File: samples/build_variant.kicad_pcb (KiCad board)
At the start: 2 copper layers, 25 x 12 mm, 2 parts

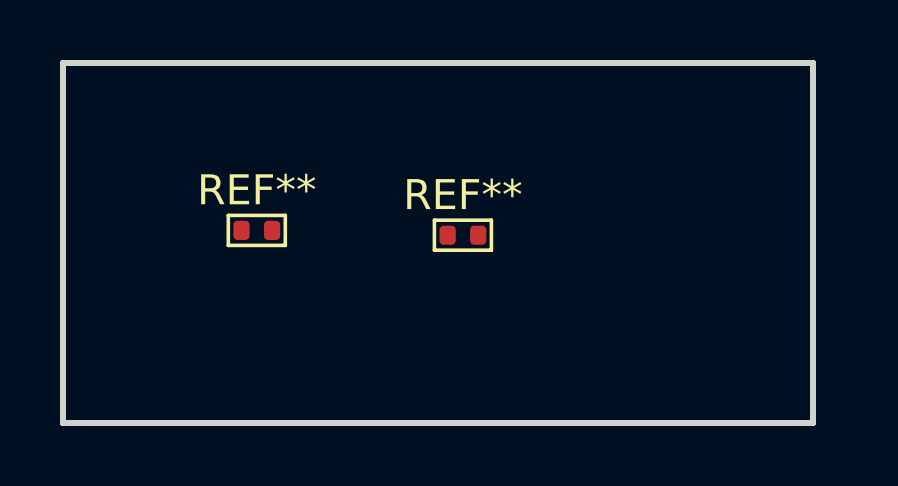
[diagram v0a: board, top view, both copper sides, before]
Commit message: Implement StringTemplate footprint & formatting
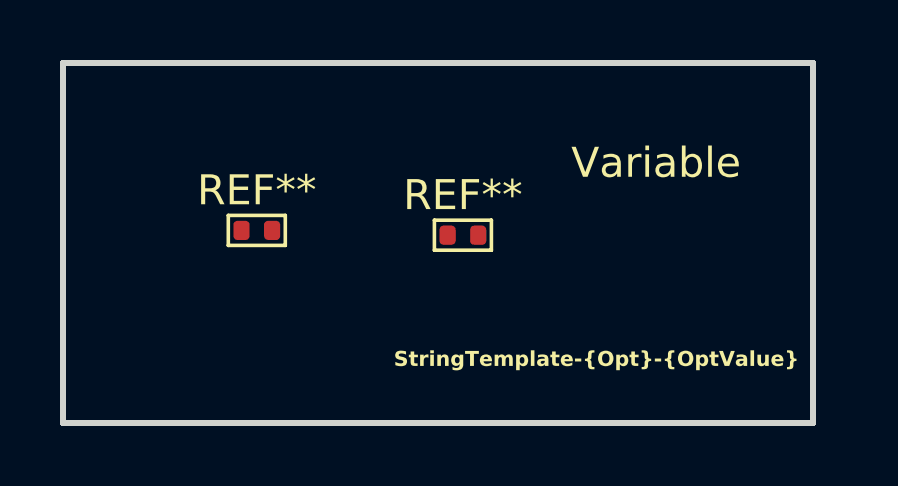
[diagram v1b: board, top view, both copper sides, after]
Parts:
- added REF**: StringTemplate-{Opt}-{OptValue}, Kikakuka:StringTemplate, F.Cu at (117.8, 109.9)
- added REF**: Variable, Kikakuka:Variable, F.Cu at (119.8, 103.3)
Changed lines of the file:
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@@
 (kicad_pcb
-	(version 20241229)
+	(version 20260206)
 	(generator "pcbnew")
-	(generator_version "9.0")
+	(generator_version "10.0")
 	(general
 		(thickness 1.6)
@@
 		(pad_to_mask_clearance 0)
 		(allow_soldermask_bridges_in_footprints no)
-		(tenting front back)
+		(tenting
+			(front yes)
+			(back yes)
+		)
+		(covering
+			(front no)
+			(back no)
+		)
+		(plugging
+			(front no)
+			(back no)
+		)
+		(capping no)
+		(filling no)
 		(pcbplotparams
 			(layerselection 0x00000000_00000000_55555555_5755f5ff)
@@
 			(usegerberadvancedattributes yes)
 			(creategerberjobfile yes)
-			(dashed_line_dash_ratio 12.000000)
-			(dashed_line_gap_ratio 3.000000)
+			(dashed_line_dash_ratio 12)
+			(dashed_line_gap_ratio 3)
 			(svgprecision 4)
 			(plotframeref no)
 			(mode 1)
 			(useauxorigin no)
-			(hpglpennumber 1)
-			(hpglpenspeed 20)
-			(hpglpendiameter 15.000000)
 			(pdf_front_fp_property_popups yes)
 			(pdf_back_fp_property_popups yes)
@@
 		)
 	)
-	(net 0 "")
 	(footprint "PCM_Resistor_SMD_AKL:R_0402_1005Metric"
 		(layer "F.Cu")
@@
 		)
 		(attr smd)
+		(duplicate_pad_numbers_are_jumpers no)
 		(fp_line
 			(start -0.95 -0.5)
@@
 		)
 		(embedded_fonts no)
-		(model "${KICAD6_3DMODEL_DIR}/Resistor_SMD.3dshapes/R_0402_1005Metric.wrl"
+		(model "${KICAD10_3DMODEL_DIR}/Resistor_SMD.3dshapes/R_0402_1005Metric.step"
 			(offset
 				(xyz 0 0 0)
@@
 			)
 		)
+	)
+	(footprint "Kikakuka:StringTemplate"
+		(layer "F.Cu")
+		(at 117.78 109.86625)
+		(property "Reference" "REF**"
+			(at 0 -0.5 0)
+			(unlocked yes)
+			(layer "F.SilkS")
+			(hide yes)
+			(effects
+				(font
+					(size 1 1)
+					(thickness 0.1)
+				)
+			)
+		)
+		(property "Value" "StringTemplate-{Opt}-{OptValue}"
+			(at 0 0 0)
+			(unlocked yes)
+			(layer "F.SilkS")
+			(effects
+				(font
+					(size 0.5 0.5)
+					(thickness 0.1)
+					(bold yes)
+				)
+			)
+		)
+		(property "Datasheet" ""
+			(at 0 0 0)
+			(unlocked yes)
+			(layer "F.Fab")
+			(hide yes)
+			(effects
+				(font
+					(size 1 1)
+					(thickness 0.15)
+				)
+			)
+		)
+		(property "Description" ""
+			(at 0 0 0)
+			(unlocked yes)
+			(layer "F.Fab")
+			(hide yes)
+			(effects
+				(font
+					(size 1 1)
+					(thickness 0.15)
+				)
+			)
+		)
+		(property "OptValue#Opt=S1" "V1"
+			(at 0 0 0)
+			(unlocked yes)
+			(layer "F.Fab")
+			(hide yes)
+			(effects
+				(font
+					(size 1 1)
+					(thickness 0.15)
+				)
+			)
+		)
+		(property "OptValue#Opt=S2" "V2"
+			(at 0 0 0)
+			(unlocked yes)
+			(layer "F.Fab")
+			(hide yes)
+			(effects
+				(font
+					(size 1 1)
+					(thickness 0.15)
+				)
+			)
+		)
+		(attr smd)
+		(duplicate_pad_numbers_are_jumpers no)
+		(embedded_fonts no)
+	)
+	(footprint "Kikakuka:Variable"
+		(layer "F.Cu")
+		(at 119.77 103.33)
+		(property "Reference" "REF**"
+			(at 0 -0.5 0)
+			(unlocked yes)
+			(layer "F.SilkS")
+			(hide yes)
+			(effects
+				(font
+					(size 1 1)
+					(thickness 0.1)
+				)
+			)
+		)
+		(property "Value" "Variable"
+			(at 0 0 0)
+			(unlocked yes)
+			(layer "F.SilkS")
+			(effects
+				(font
+					(size 1 1)
+					(thickness 0.15)
+				)
+			)
+		)
+		(property "Datasheet" ""
+			(at 0 0 0)
+			(unlocked yes)
+			(layer "F.Fab")
+			(hide yes)
+			(effects
+				(font
+					(size 1 1)
+					(thickness 0.15)
+				)
+			)
+		)
+		(property "Description" ""
+			(at 0 0 0)
+			(unlocked yes)
+			(layer "F.Fab")
+			(hide yes)
+			(effects
+				(font
+					(size 1 1)
+					(thickness 0.15)
+				)
+			)
+		)
+		(property "Value#Opt=S1" "V1"
+			(at 0 0 0)
+			(unlocked yes)
+			(layer "F.Fab")
+			(hide yes)
+			(effects
+				(font
+					(size 1 1)
+					(thickness 0.15)
+				)
+			)
+		)
+		(property "Value#Opt=S2" "V2"
+			(at 0 0 0)
+			(unlocked yes)
+			(layer "F.Fab")
+			(hide yes)
+			(effects
+				(font
+					(size 1 1)
+					(thickness 0.15)
+				)
+			)
+		)
+		(attr smd)
+		(duplicate_pad_numbers_are_jumpers no)
+		(embedded_fonts no)
 	)
 	(footprint "PCM_Resistor_SMD_AKL:R_0402_1005Metric"
@@
 		)
 		(attr smd)
+		(duplicate_pad_numbers_are_jumpers no)
 		(fp_line
 			(start -0.95 -0.5)
@@
 		)
 		(embedded_fonts no)
-		(model "${KICAD6_3DMODEL_DIR}/Resistor_SMD.3dshapes/R_0402_1005Metric.wrl"
+		(model "${KICAD10_3DMODEL_DIR}/Resistor_SMD.3dshapes/R_0402_1005Metric.step"
 			(offset
 				(xyz 0 0 0)
